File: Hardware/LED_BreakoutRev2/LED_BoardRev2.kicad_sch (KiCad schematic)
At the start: 44 parts

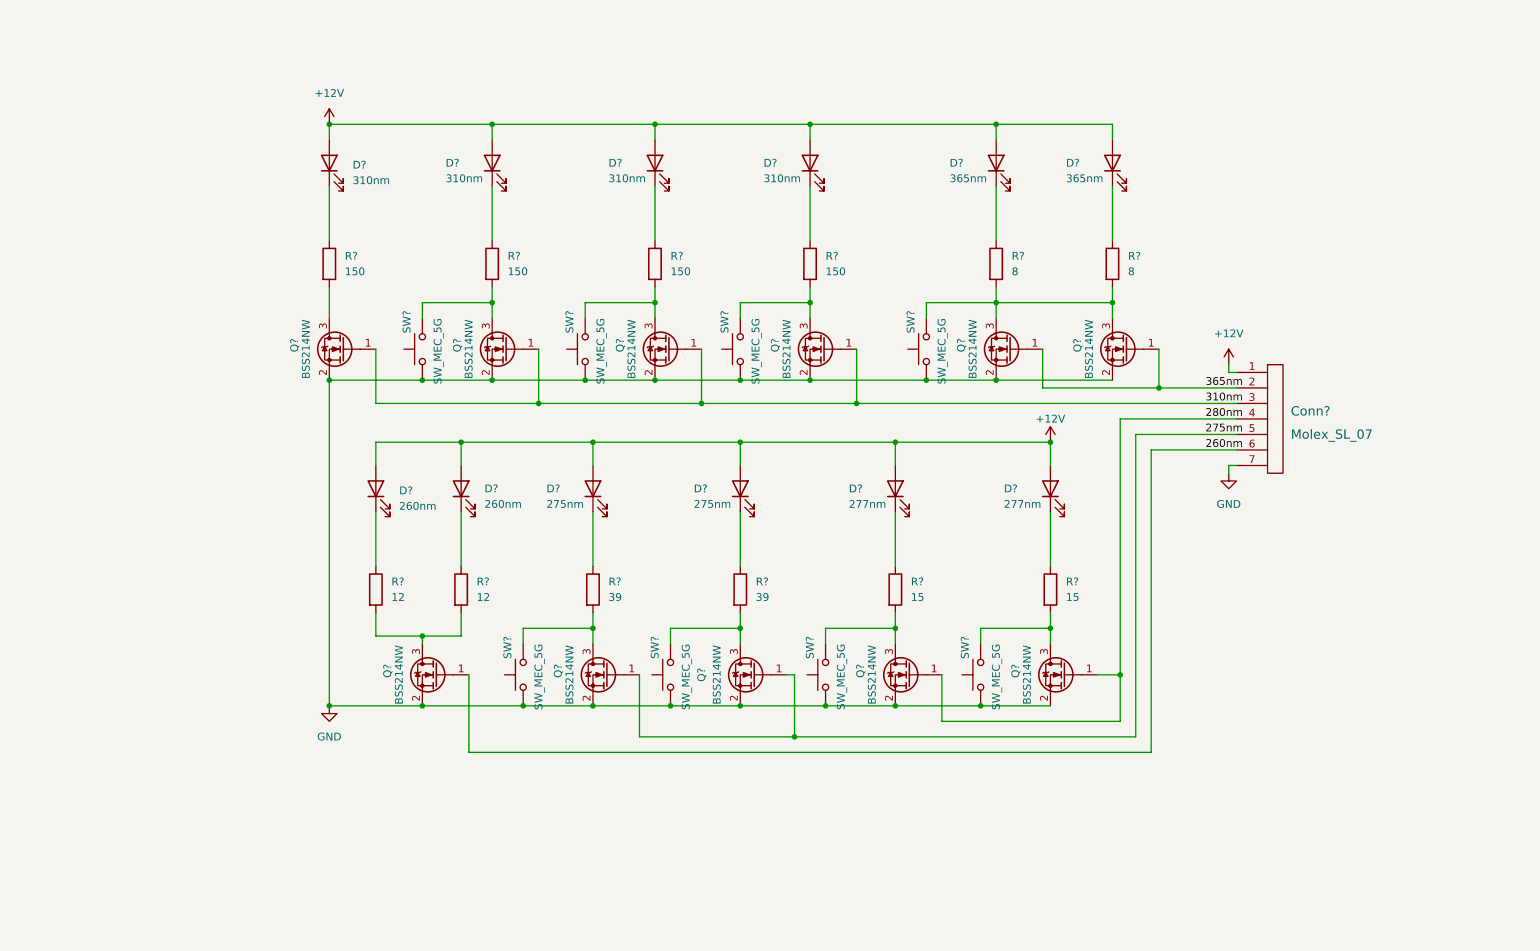
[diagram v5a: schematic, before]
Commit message: Finished  LED Schematic
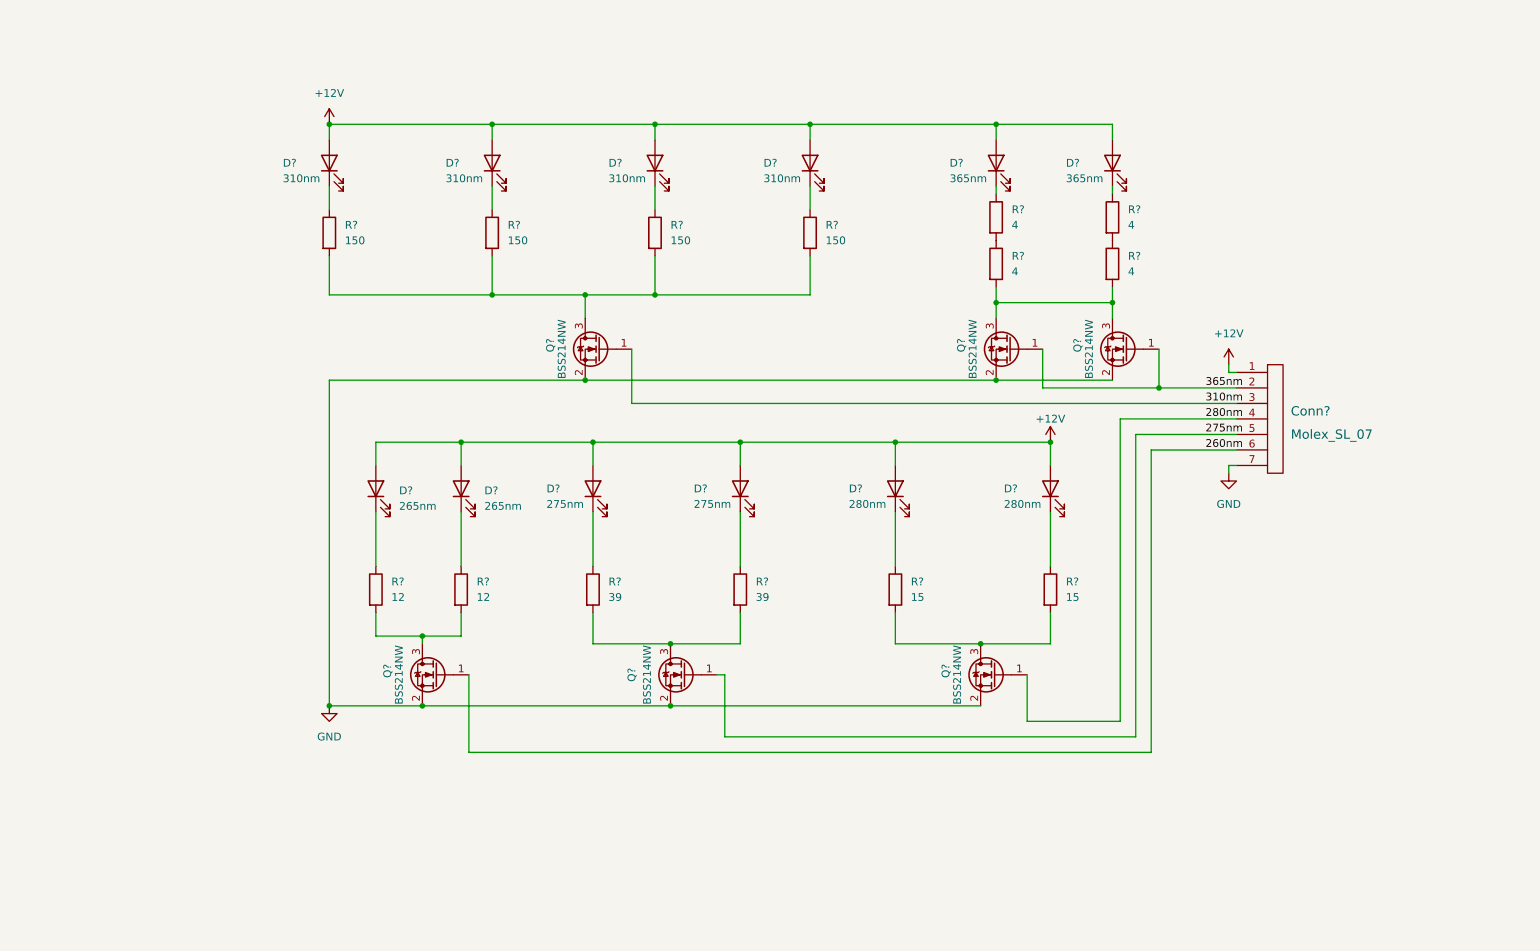
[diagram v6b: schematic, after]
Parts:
- removed D?: 277nm, MRDT_Devices:280nm, symbol Device:LED
- removed D?: 260nm, KL265-50W-SM-WD Footprint:3535, symbol Device:LED
- removed D?: 365nm, symbol Device:LED
- removed D? (x3): 310nm, MRDT_Devices:310nm, symbol Device:LED
- removed Q? (x5): BSS214NW, Package_TO_SOT_SMD:SOT-323_SC-70, symbol Transistor_FET:BSS214NW
- removed R?: 12, symbol Device:R
- removed R? (x3): 150, symbol Device:R
- removed R?: 8, symbol Device:R
- removed R?: 15, symbol Device:R
- removed R?: 39, symbol Device:R
- removed SW? (x8): SW_MEC_5G, symbol Switch:SW_MEC_5G
- added D? (x3): 310nm, MRDT_Devices:310nm, symbol Device:LED
- added D?: 280nm, MRDT_Devices:280nm, symbol Device:LED
- added D?: 365nm, MRDT_Devices:365nm LED, symbol Device:LED
- added D?: 265nm, KL265-50W-SM-WD Footprint:3535, symbol Device:LED
- added R?: 15, Resistor_SMD:R_2512_6332Metric_Pad1.40x3.35mm_HandSolder, symbol Device:R
- added R? (x3): 150, Resistor_SMD:R_2512_6332Metric_Pad1.40x3.35mm_HandSolder, symbol Device:R
- added R?: 39, Resistor_SMD:R_2512_6332Metric_Pad1.40x3.35mm_HandSolder, symbol Device:R
- added R?: 12, Resistor_SMD:R_2512_6332Metric_Pad1.40x3.35mm_HandSolder, symbol Device:R
- added R? (x3): 4, MRDT_Devices:Stupid 4 Ohm Resistor, symbol Device:R
- D?: footprint (none) -> MRDT_Devices:365nm LED
- D?: value 260nm -> 265nm
- D?: value 277nm -> 280nm
- R? (x4): footprint (none) -> Resistor_SMD:R_2512_6332Metric_Pad1.40x3.35mm_HandSolder
- R?: value 8 -> 4; footprint (none) -> MRDT_Devices:Stupid 4 Ohm Resistor
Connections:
- net +12V: now also D?.2 (A), D?.2 (A), D?.2 (A), D?.2 (A), D?.2 (A), D?.2 (A)
- net at Q?.3 (D), R?.2: now also R?.2
- net at R?.1: now also D?.1 (K)
- net at R?.2: now also Q?.3 (D), R?.2, R?.2, R?.2
- net at D?.1 (K): now also R?.1; no longer R?.1
- net at D?.1 (K): now also R?.1 (x2)
- net at Q?.3 (D), Q?.3 (D), R?.2: now also R?.2
- net at R?.2: now also Q?.3 (D), R?.2 (x2)
- new net: D?.1 (K), R?.1 (x5)
- new net: R?.1, R?.2 (x2)
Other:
- moved on the sheet: Q?, R?

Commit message: Began Layout
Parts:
- Conn1: renamed from Conn?; footprint (none) -> MRDT_Connectors:MOLEX_SL_07_Vertical
- gave numbers to parts that had none: 32

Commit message: adjusted resistor values
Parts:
- R1: value 150 -> 250
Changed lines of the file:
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@@
       (effects (font (size 1.27 1.27)) (justify left))
     )
-    (property "Value" "150" (id 1) (at 83.82 52.0699 0)
+    (property "Value" "250" (id 1) (at 83.82 52.0699 0)
       (effects (font (size 1.27 1.27)) (justify left))
     )
@@
     )
     (path "/00ffef87-41ab-498e-a52c-9e3f66475947"
-      (reference "R1") (unit 1) (value "150") (footprint "Resistor_SMD:R_2512_6332Metric_Pad1.40x3.35mm_HandSolder")
+      (reference "R1") (unit 1) (value "250") (footprint "Resistor_SMD:R_2512_6332Metric_Pad1.40x3.35mm_HandSolder")
     )
     (path "/1fa96d35-89d1-48e4-b862-0f8f9ffc3ff2"
